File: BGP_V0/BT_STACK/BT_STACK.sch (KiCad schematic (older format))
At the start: 13 parts, among them P1 CONN_01X05, U1 OPA180

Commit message: Pot fixups for silkscreen overlap
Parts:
- RV1: footprint LIBS:Potentiometer_Alpha_Double_Vertical_Dual_Shaft -> LIBS:Potentiometer_Alps_RK097_Double_Vertical_Dual_Shaft
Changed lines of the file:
@@
 F 0 "RV1" H 5460 5510 50  0000 C CNN
 F 1 "DUAL_POT" H 5590 4900 50  0000 C CNN
-F 2 "LIBS:Potentiometer_Alpha_Double_Vertical_Dual_Shaft" H 5300 5200 50  0001 C CNN
+F 2 "LIBS:Potentiometer_Alps_RK097_Double_Vertical_Dual_Shaft" H 5300 5200 50  0001 C CNN
 F 3 "" H 5300 5200 50  0000 C CNN
 	1    5300 5200

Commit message: V_0 Updates for caps, gerbers updated
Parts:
- C1: footprint Capacitors_Tantalum_SMD:TantalC_SizeB_EIA-3528_HandSoldering -> Capacitors_SMD:C_0805_HandSoldering
- C5: footprint Capacitors_SMD:C_1210_HandSoldering -> Capacitors_SMD:C_0805_HandSoldering
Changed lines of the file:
@@
 F 0 "C1" H 4410 2520 50  0000 L CNN
 F 1 "22u" H 4410 2370 50  0000 L CNN
-F 2 "Capacitors_Tantalum_SMD:TantalC_SizeB_EIA-3528_HandSoldering" H 4400 2450 50  0001 C CNN
+F 2 "Capacitors_SMD:C_0805_HandSoldering" H 4400 2450 50  0001 C CNN
 F 3 "" H 4400 2450 50  0000 C CNN
 	1    4400 2450
@@
 F 0 "C5" H 5560 3570 50  0000 L CNN
 F 1 "0.1u" H 5560 3420 50  0000 L CNN
-F 2 "Capacitors_SMD:C_1210_HandSoldering" H 5550 3500 50  0001 C CNN
+F 2 "Capacitors_SMD:C_0805_HandSoldering" H 5550 3500 50  0001 C CNN
 F 3 "" H 5550 3500 50  0000 C CNN
 	1    5550 3500

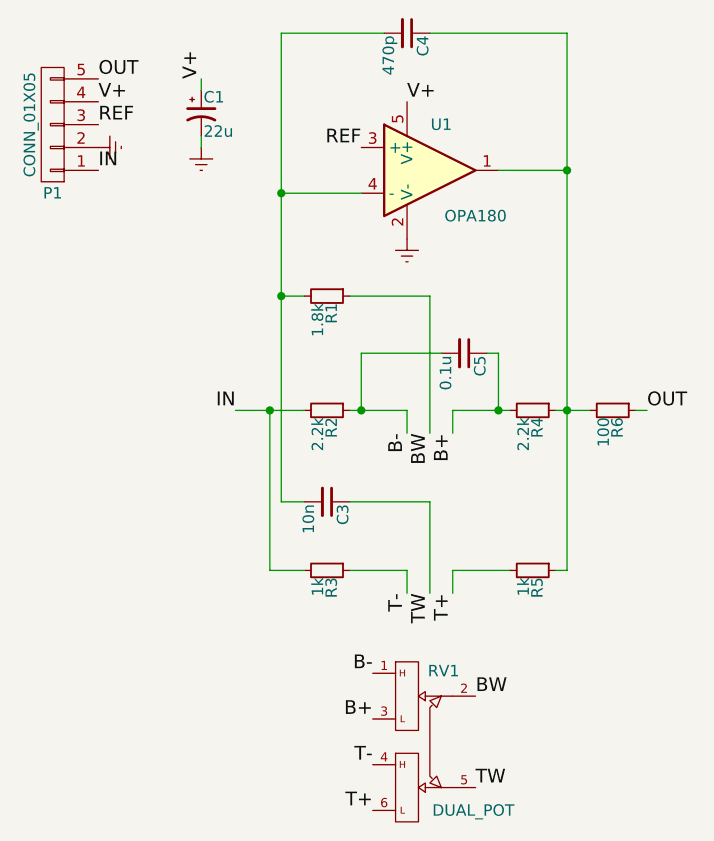
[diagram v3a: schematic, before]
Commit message: V0 BUF and BT Edits
V0 Buffer change from CRD to JFET CCS. BT stack changed to reflect +/- 9V changes.
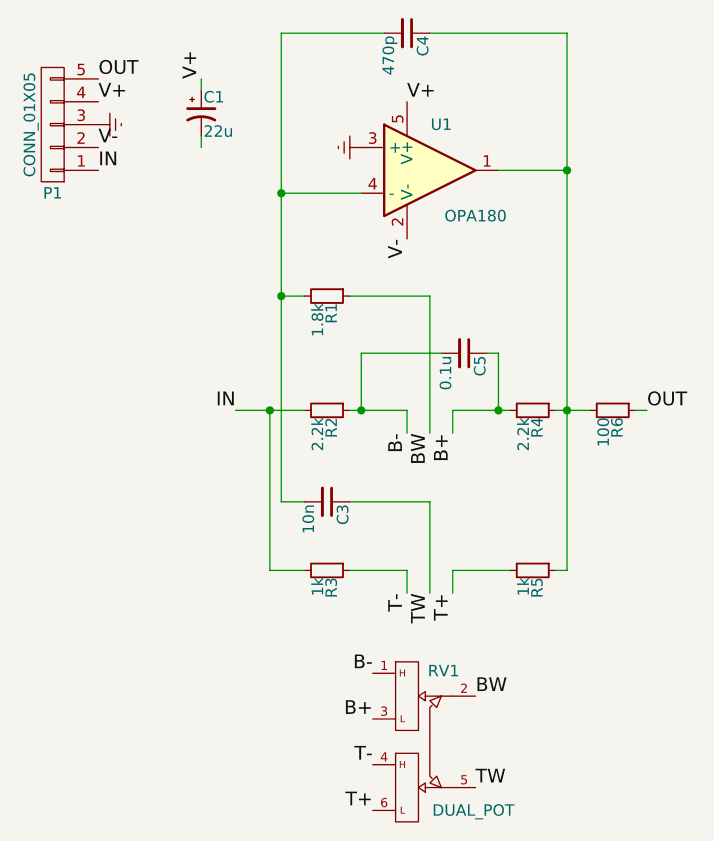
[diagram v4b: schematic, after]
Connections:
- net REF is gone; now on net Earth: P1.3 (P3), U1.3 (+)
- net Earth: no longer C1.2, P1.2 (P2), U1.2 (V-)
- new net V-: P1.2 (P2), U1.2 (V-)
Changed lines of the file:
@@
-	1    0    0    -1
-$EndComp
-$Comp
-L Earth #PWR01
-U 1 1 5A28872E
-P 4400 2600
-F 0 "#PWR01" H 4400 2350 50  0001 C CNN
-F 1 "Earth" H 4400 2450 50  0001 C CNN
-F 2 "" H 4400 2600 50  0000 C CNN
-F 3 "" H 4400 2600 50  0000 C CNN
-	1    4400 2600
 	1    0    0    -1
 $EndComp
@@
 Text Label 5300 2400 0    60   ~ 0
 V+
-$Comp
-L Earth #PWR02
-U 1 1 5A28886E
-P 5300 3000
-F 0 "#PWR02" H 5300 2750 50  0001 C CNN
-F 1 "Earth" H 5300 2850 50  0001 C CNN
-F 2 "" H 5300 3000 50  0000 C CNN
-F 3 "" H 5300 3000 50  0000 C CNN
-	1    5300 3000
-	1    0    0    -1
-$EndComp
-Text Label 5100 2600 2    60   ~ 0
-REF
 $Comp
 L C_Small C4
@@
 Text Label 5600 5400 0    60   ~ 0
 TW
-$Comp
-L Earth #PWR03
-U 1 1 5A28A63A
-P 3950 2600
-F 0 "#PWR03" H 3950 2350 50  0001 C CNN
-F 1 "Earth" H 3950 2450 50  0001 C CNN
-F 2 "" H 3950 2600 50  0000 C CNN
-F 3 "" H 3950 2600 50  0000 C CNN
-	1    3950 2600
-	0    -1   -1   0
-$EndComp
 Text Label 3950 2400 0    60   ~ 0
 V+
-Text Label 3950 2500 0    60   ~ 0
-REF
 Text Label 3950 2300 0    60   ~ 0
 OUT
@@
 	-1   0    0    1
 $EndComp
+Text Label 3950 2600 0    60   ~ 0
+V-
+$Comp
+L Earth #PWR?
+U 1 1 5A5AEE2D
+P 3950 2500
+F 0 "#PWR?" H 3950 2250 50  0001 C CNN
+F 1 "Earth" H 3950 2350 50  0001 C CNN
+F 2 "" H 3950 2500 50  0001 C CNN
+F 3 "" H 3950 2500 50  0001 C CNN
+	1    3950 2500
+	0    -1   -1   0
+$EndComp
+$Comp
+L Earth #PWR?
+U 1 1 5A5AEE90
+P 5100 2600
+F 0 "#PWR?" H 5100 2350 50  0001 C CNN
+F 1 "Earth" H 5100 2450 50  0001 C CNN
+F 2 "" H 5100 2600 50  0001 C CNN
+F 3 "" H 5100 2600 50  0001 C CNN
+	1    5100 2600
+	0    1    1    0
+$EndComp
+Text Label 5300 3000 3    60   ~ 0
+V-
 $EndSCHEMATC

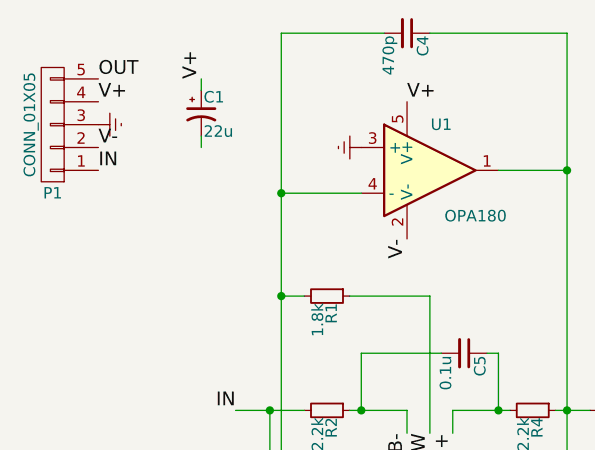
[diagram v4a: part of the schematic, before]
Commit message: Reduced BT MID board sizes.
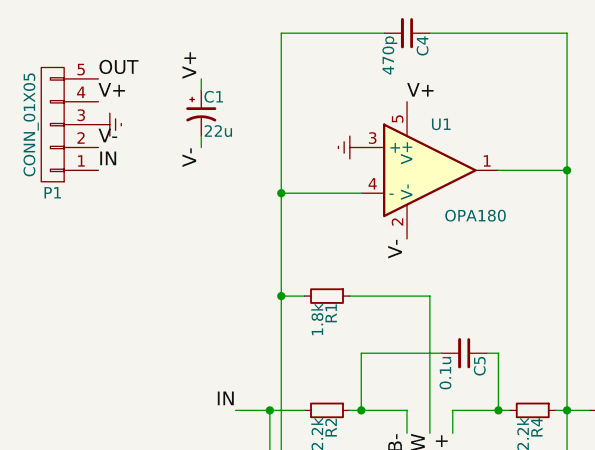
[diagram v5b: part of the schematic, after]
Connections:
- net V-: now also C1.2
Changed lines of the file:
@@
 Text Label 5300 3000 3    60   ~ 0
 V-
+Text Label 4400 2600 3    60   ~ 0
+V-
 $EndSCHEMATC
